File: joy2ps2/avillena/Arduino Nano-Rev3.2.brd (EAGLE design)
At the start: 43.2 x 17.8 mm, 31 parts, among them IC1 FT232RL, IC2 LM1117IMPX-5.0, IC3 ATMEGA328P-AU, J1 XXXX_STRIPNANO, J2 XXXX_STRIPNANO, SW1 RESET, Y1 16MHz

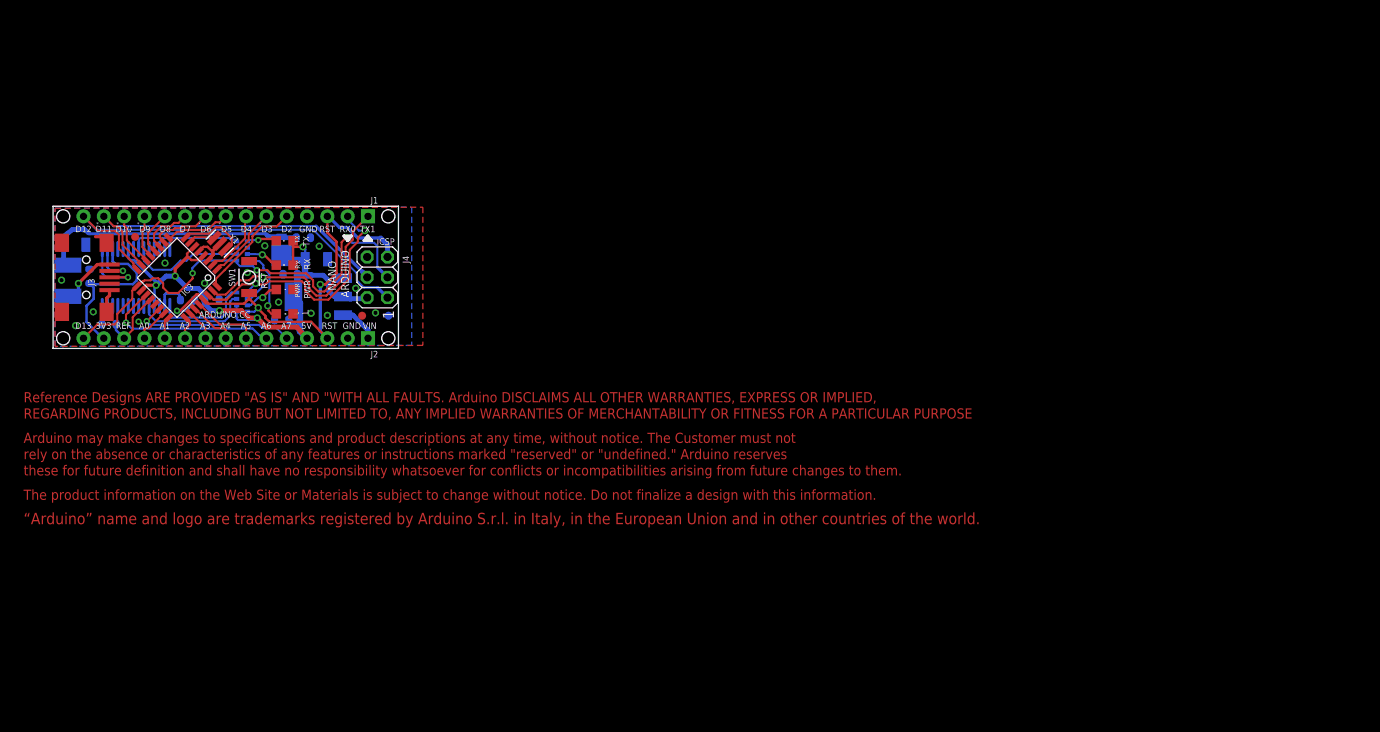
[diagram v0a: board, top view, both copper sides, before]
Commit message: Añado al Arduino nano componentes del gamepad
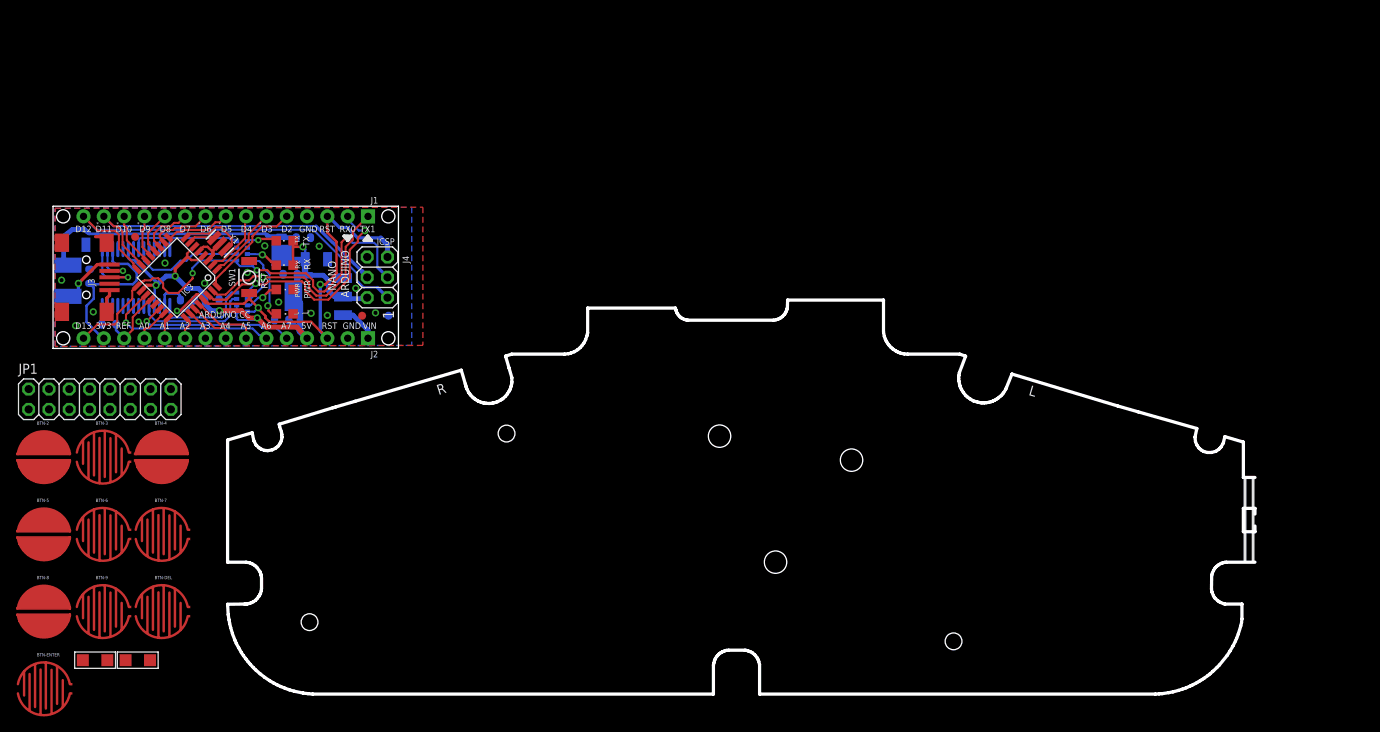
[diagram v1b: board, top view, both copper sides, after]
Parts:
- removed U$5: DISCLAIMER-SMALL, Misc:DISCLAIMER
- added BTN-0: L, ,giltesa:1X02_SMD
- added BTN-1: R, ,giltesa:1X02_SMD
- added BTN-2: UP, ,giltesa:BUTTON-CONDUCTIVE-PAD
- added BTN-3: X, ,giltesa:BUTTON-CONDUCTIVE-BUTTON
- added BTN-4: LEFT, ,giltesa:BUTTON-CONDUCTIVE-PAD
- added BTN-5: RIGHT, ,giltesa:BUTTON-CONDUCTIVE-PAD
- added BTN-6: A, ,giltesa:BUTTON-CONDUCTIVE-BUTTON
- added BTN-7: Y, ,giltesa:BUTTON-CONDUCTIVE-BUTTON
- added BTN-8: DOWN, ,giltesa:BUTTON-CONDUCTIVE-PAD
- added BTN-9: B, ,giltesa:BUTTON-CONDUCTIVE-BUTTON
- added BTN-DEL: SLECT, ,giltesa:BUTTON-CONDUCTIVE-BUTTON
- added BTN-ENTER: START, ,giltesa:BUTTON-CONDUCTIVE-BUTTON
- added JP1: (no value), pinhead:2X08
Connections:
- new net COL1: BTN-1.1, BTN-DEL.2
- new net COL2: BTN-2.2
- new net COL3: BTN-3.1
- new net COL4: BTN-4.1, BTN-ENTER.1
- new net COL5: BTN-0.1, BTN-5.2
- new net COL6: BTN-6.2, BTN-8.2, BTN-9.2
- new net COL7: BTN-7.2
- new net FIL1: BTN-1.2, BTN-2.1, BTN-3.2, BTN-4.2, BTN-5.1, BTN-6.1, BTN-7.1
- new net FIL2: BTN-8.1, BTN-DEL.1
- new net FIL3: BTN-0.2, BTN-9.1
- new net FIL4: BTN-ENTER.2
- new net GND: JP1.1
- new net N$10: JP1.3
- new net N$12: JP1.5
- new net N$13: JP1.7
- new net N$14: JP1.9
- new net N$15: JP1.11
- new net N$16: JP1.13
- new net N$17: JP1.15
- new net N$18: JP1.2
- new net N$19: JP1.4
- new net N$20: JP1.6
- new net N$21: JP1.8
- new net N$22: JP1.10
- new net N$23: JP1.12
- new net N$24: JP1.14
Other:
- board size 43.2 x 17.8 mm -> 150.2 x 61 mm
- board text added: "A"
- board text added: "B"
- board text added: "Down"
- board text added: "Left"
- board text added: "R"
- board text added: "Right"
- board text added: "Select"
- board text added: "Start"
- board text added: "Up"
- board text added: "X"

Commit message: Hago commit de lo último
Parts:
- removed C4, C6: 100nF, Condensatori:C0603-ROUND
- removed F1: MF-MSMF050-2 500mA, Protezione:L1812
- removed IC1: FT232RL, IntegratedCircuits:SSOP28
- removed J3: (no value), Connettori:USB-MINI-B_2
- removed RX: Red, Opto:CHIPLED_0805
- removed TX: Green, Opto:CHIPLED_0805
- moved BTN-2 128.3 mm to (127.1, -13.2), flipped to the bottom
- moved BTN-8 128.0 mm to (126.9, -31.5), flipped to the bottom
- moved BTN-4 122.3 mm to (135.6, -22.0), flipped to the bottom
- moved BTN-5 118.5 mm to (117.3, -22.0), flipped to the bottom
- moved BTN-0 111.2 mm to (112.3, -8.89)
- moved BTN-ENTER 85.2 mm to (82.5, -26.4), flipped to the bottom
- moved BTN-DEL 84.2 mm to (97.5, -26.5), flipped to the bottom
- moved BTN-1 60.9 mm to (62.5, -7.11)
- moved BTN-7 44.1 mm to (57.7, -22.5), flipped to the bottom
- moved BTN-3 38.5 mm to (44.7, -11.6), flipped to the bottom
- moved BTN-9 37.6 mm to (43.8, -32.9), flipped to the bottom
- moved BTN-6 25.4 mm to (31.6, -22.2), flipped to the bottom
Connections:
- removed net GND: JP1.1
- removed net N$10: JP1.3
- removed net N$11: RP2.5, TX.C
- removed net N$12: JP1.5
- removed net N$13: JP1.7
- removed net N$14: JP1.9
- removed net N$15: JP1.11
- removed net N$16: JP1.13
- removed net N$17: JP1.15
- removed net N$18: JP1.2
- removed net N$19: JP1.4
- removed net N$20: JP1.6
- removed net N$21: JP1.8
- removed net N$22: JP1.10
- removed net N$23: JP1.12
- removed net N$24: JP1.14
- removed net N$26: F1.2, J3.5
- removed net N$29: RP2.7, RX.C
- removed net N$4: C4.2, IC1.2
- removed net N$5: IC1.15, J3.3
- removed net N$6: IC1.16, J3.4
- removed net N$8: IC1.23, RP2.2
- removed net N$9: IC1.22, RP2.4
- net +5V: now also JP1.8; no longer IC1.20, IC1.4, RX.A, TX.A
- net 3V3: no longer C6.2, IC1.17
- net A3: now also JP1.9
- net A4: now also JP1.15
- net A5: now also JP1.7
- net COM: now also JP1.1; no longer C6.1, IC1.18, IC1.21, IC1.25, IC1.26, IC1.7, J3.1, J3.6, J3.7, J3.8, J3.9
- net D10: now also JP1.10
- net D11/MOSI: now also JP1.2
- net D2: now also JP1.14
- net D3: now also JP1.6
- net D4: now also JP1.13
- net D5: now also JP1.5
- net D6: now also JP1.12
- net D7: now also JP1.4
- net D8: now also JP1.11
- net D9: now also JP1.3
- net RESET: no longer C4.1
- net RX: no longer IC1.1
- net TX: no longer IC1.5
- net VUSB: no longer F1.1
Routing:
- net N$8: track 14.4 -> 0.00 mm
- net N$9: track 13.7 -> 0.00 mm
- net 3V3: track 20.6 -> 7.69 mm
- net N$5: track 9.08 -> 0.00 mm, vias 1 -> 0
- net N$26: track 7.99 -> 0.00 mm, vias 1 -> 0
- net N$6: track 6.23 -> 0.00 mm, vias 1 -> 0
- net COM: track 10.4 -> 5.42 mm
- net +5V: track 81.8 -> 77.6 mm
- net N$29: track 4.22 -> 0.00 mm, vias 1 -> 0
- net N$4: track 4.07 -> 0.00 mm
- net N$11: track 3.91 -> 0.00 mm, vias 1 -> 0
- net RX: track 12.1 -> 10.8 mm
- net TX: track 14.5 -> 13.5 mm

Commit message: Avanzo diseño
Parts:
- removed J1, J2: XXXX_STRIPNANO, Connettori:HEAD15-NOSS
- removed U$37, U$4, U$53, U$54: FIDUCIAL1X2, SparkFun:FIDUCIAL-1X2
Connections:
- removed net 3V3: J2.14
- removed net COL1: BTN-1.1, BTN-DEL.2
- removed net COL2: BTN-2.2
- removed net COL3: BTN-3.1
- removed net COL4: BTN-4.1, BTN-ENTER.1
- removed net COL5: BTN-0.1, BTN-5.2
- removed net COL6: BTN-6.2, BTN-8.2, BTN-9.2
- removed net COL7: BTN-7.2
- removed net FIL1: BTN-1.2, BTN-2.1, BTN-3.2, BTN-4.2, BTN-5.1, BTN-6.1, BTN-7.1
- removed net FIL2: BTN-8.1, BTN-DEL.1
- removed net FIL3: BTN-0.2, BTN-9.1
- removed net FIL4: BTN-ENTER.2
- new net GND: BTN-0.1, BTN-1.1, BTN-2.2, BTN-3.1, BTN-4.1, BTN-5.2, BTN-6.2, BTN-7.2, BTN-8.2, BTN-9.2, BTN-DEL.2, BTN-ENTER.1
- net +5V: no longer J2.4
- net A0: no longer J2.12
- net A1: no longer J2.11
- net A2: no longer J2.10
- net A3: no longer J2.9
- net A4: now also BTN-2.1; no longer J2.8
- net A5: now also BTN-8.1; no longer J2.7
- net A6: no longer J2.6
- net A7: no longer J2.5
- net AREF: no longer J2.13
- net COM: no longer J1.4, J2.2
- net D0/RX: no longer J1.2
- net D1/TX: no longer J1.1
- net D10: now also BTN-0.2; no longer J1.13
- net D11/MOSI: now also BTN-1.2; no longer J1.14
- net D12/MISO: no longer J1.15
- net D13/SCK: no longer J2.15
- net D2: now also BTN-4.2; no longer J1.5
- net D3: now also BTN-5.1; no longer J1.6
- net D4: now also BTN-6.1; no longer J1.7
- net D5: now also BTN-9.1; no longer J1.8
- net D6: now also BTN-3.2; no longer J1.9
- net D7: now also BTN-7.1; no longer J1.10
- net D8: now also BTN-ENTER.2; no longer J1.11
- net D9: now also BTN-DEL.1; no longer J1.12
- net RESET: no longer J1.3, J2.3
- net VIN: no longer J2.1
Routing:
- net RESET: track 56.7 -> 36.3 mm, vias 3 -> 2
- net 3V3: track 7.69 -> 0.00 mm
- net D12/MISO: track 53.4 -> 48.5 mm
- net D11/MOSI: track 44.7 -> 41.2 mm
- net +5V: track 77.6 -> 74.4 mm
- net D3: track 9.37 -> 6.25 mm
- net D8: track 5.87 -> 2.92 mm
- net AREF: track 8.76 -> 5.82 mm
- net D1/TX: track 33.3 -> 30.6 mm
- net D13/SCK: track 57.1 -> 54.7 mm
- net A1: track 2.84 -> 0.71 mm
- net A7: track 21.0 -> 19.2 mm
- net D2: track 13.5 -> 11.7 mm
- net D6: track 8.11 -> 6.35 mm
- net D9: track 5.75 -> 4.30 mm
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- removed copper zone on layer 1, net COM
- removed copper zone on layer 16, net COM
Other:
- board size 150.2 x 61 mm -> 128.4 x 49.3 mm

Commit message: A falta de vías
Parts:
- removed C2: 4,7uF_16V, Condensatori:TAN-A
- removed C8: 1uF, Condensatori:C0603-ROUND
- removed C9: 100nF, Condensatori:C0603-ROUND
- removed D1: SS1P3L, Diodi:DO220AAL
- removed IC2: LM1117IMPX-5.0, IntegratedCircuits:LINEAR_SOT223
- removed J4: (no value), Connettori:2X03
- removed PWR: Green, Opto:CHIPLED_0805
- removed RP2: 1K, Resistenze:CAY16
- removed SW1: RESET, Switches:SMD_157SW
- added JP2: (no value), pinhead:2X05
- JP1: device pinhead:2X08 -> pinhead:2X07
- moved JP1 61.5 mm to (57.0, 27.8)
- moved BTN-3 48.4 mm to (24.6, 32.5)
- moved BTN-4 48.4 mm to (115.6, 22.1)
- moved BTN-5 48.4 mm to (97.3, 22.1)
- moved BTN-6 48.4 mm to (11.6, 21.8)
- moved BTN-7 48.4 mm to (37.6, 21.6)
- moved BTN-8 48.4 mm to (106.8, 12.6)
- moved BTN-9 48.4 mm to (23.7, 11.2)
- moved BTN-DEL 48.4 mm to (77.5, 17.5)
- moved BTN-ENTER 48.4 mm to (62.5, 17.7)
- moved BTN-2 48.4 mm to (107.1, 30.9)
- moved BTN-0 48.1 mm to (89.5, 33.5)
- moved BTN-1 44.3 mm to (42.4, 32.4), turned to 180 degrees
- moved C3 41.4 mm to (58.7, 20.5), flipped to the top, turned to 90 degrees
- moved C1 37.5 mm to (44.2, 7.72), flipped to the top
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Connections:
- removed net COM: C1.2, C2.2, C3.2, C5.2, C7.2, C8.2, C9.2, IC2.1, IC3.21, IC3.3, IC3.5, J4.6, JP1.1, L.C, PWR.C, RP2.3, RP2.6, SW1.1, Y1.2
- removed net N$3: PWR.A, RP1.3
- removed net VIN: IC2.3
- removed net VUSB: C2.1, C9.1, D1.P$2
- net +5V: now also JP2.7; no longer C8.1, D1.P$1, IC2.2, IC2.4, J4.2, RP1.5
- net A2: now also JP2.1
- net A3: now also JP2.3; no longer JP1.9
- net A4: now also JP1.11; no longer JP1.15
- net A5: now also JP1.13; no longer JP1.7
- net D0/RX: now also RP1.2; no longer RP1.1
- net D1/TX: now also RP1.1; no longer RP1.2
- net D10: now also JP1.2; no longer JP1.10
- net D11/MOSI: now also JP1.10, JP2.10; no longer J4.4, JP1.2
- net D12/MISO: now also JP2.9; no longer J4.1
- net D13/SCK: now also JP2.8, RP1.4; no longer J4.3, RP2.1
- net D3: now also JP1.12; no longer JP1.6
- net D4: now also JP1.9; no longer JP1.13
- net D6: now also JP1.6; no longer JP1.12
- net D7: now also JP1.3; no longer JP1.4
- net D8: now also JP1.4; no longer JP1.11
- net D9: now also JP1.1; no longer JP1.3
- net GND: now also C1.2, C3.2, C5.2, C7.2, IC3.21, IC3.3, IC3.5, JP1.7, JP2.5, L.C, Y1.2
- net N$7: now also RP1.5; no longer RP2.8
- net RESET: now also JP2.6, RP1.3; no longer J4.5, RP1.4, SW1.2
- net RX: now also JP2.4, RP1.7; no longer RP1.8
- net TX: now also JP2.2, RP1.8; no longer RP1.7
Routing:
- net A4: track 5.63 -> 83.3 mm
- net D4: track 8.44 -> 80.9 mm
- net D2: track 11.7 -> 83.7 mm
- net D10: track 5.81 -> 74.5 mm
- net A5: track 7.49 -> 75.4 mm
- net D3: track 6.25 -> 67.1 mm
- net GND: track 0.00 -> 54.5 mm
- net D5: track 7.31 -> 52.7 mm
- net D6: track 6.35 -> 51.4 mm
- net +5V: track 74.4 -> 37.7 mm, vias 5 -> 0
- net VUSB: track 34.5 -> 0.00 mm
- net D13/SCK: track 54.7 -> 21.8 mm, vias 3 -> 0
- net RESET: track 36.3 -> 4.29 mm, vias 2 -> 0
- net D8: track 2.92 -> 32.5 mm
- net D0/RX: track 33.0 -> 4.29 mm, vias 2 -> 0
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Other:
- board size 128.4 x 49.3 mm -> 128.4 x 40.5 mm
- board text removed: "*"
- board text removed: "1"
- board text removed: "3V3"
- board text removed: "5V"
- board text removed: "A0"
- board text removed: "A1"
- board text removed: "A2"
- board text removed: "A3"
- board text removed: "A4"
- board text removed: "A5"
- board text removed: "A6"
- board text removed: "A7"
- board text removed: "ARDUINO"
- board text removed: "ARDUINO.CC"
- board text removed: "D10"
- board text removed: "D11"
- board text removed: "D12"
- board text removed: "D13"
- board text removed: "D2"
- board text removed: "D3"
- board text removed: "D4"
- board text removed: "D5"
- board text removed: "D6"
- board text removed: "D7"
- board text removed: "D8"
- board text removed: "D9"
- board text removed: "GND"
- board text removed: "ICSP"
- board text removed: "NANO"
- board text removed: "PWR"
- board text removed: "REF"
- board text removed: "RST"
- board text removed: "RX"
- board text removed: "RX0"
- board text removed: "TX"
- board text removed: "TX1"
- board text removed: "VIN"

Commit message: Versión final
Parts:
- BTN-DEL: value SLECT -> SELECT
- moved BTN-1 1.14 mm to (42.4, 33.5)
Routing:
- net GND: track 54.5 -> 284.2 mm, vias 0 -> 1
- net D11/MOSI: track 42.1 -> 142.5 mm
- net +5V: track 37.7 -> 95.5 mm, vias 0 -> 1
- net D9: track 10.5 -> 42.2 mm, vias 0 -> 1
- net D13/SCK: track 21.8 -> 46.1 mm, vias 0 -> 1
- net RESET: track 4.29 -> 24.6 mm, vias 0 -> 1
- net D10: track 74.5 -> 75.7 mm
- net D6: track 51.4 -> 50.4 mm
- added copper zone on layer 16, net GND
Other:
- board text added: "+5V"
- board text added: "B1"
- board text added: "B2"
- board text added: "B3"
- board text added: "B4"
- board text added: "B5"
- board text added: "B6"
- board text added: "DOWN"
- board text added: "GND"
- board text added: "LEFT"
- board text added: "MISO"
- board text added: "MOSI"
- board text added: "PS2CLK"
- board text added: "PS2DAT"
- board text added: "RESET"
- board text added: "RIGHT"
- board text added: "RX"
- board text added: "SCK"
- board text added: "SELECT"
- board text added: "START"
- board text added: "TX"
- board text added: "UP"
- board text added: "Y"
